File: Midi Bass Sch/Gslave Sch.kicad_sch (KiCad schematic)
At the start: 12 parts, among them J8 G SLAVE ISCP, SW6 G-slave Reset, U10 PIC16F1789

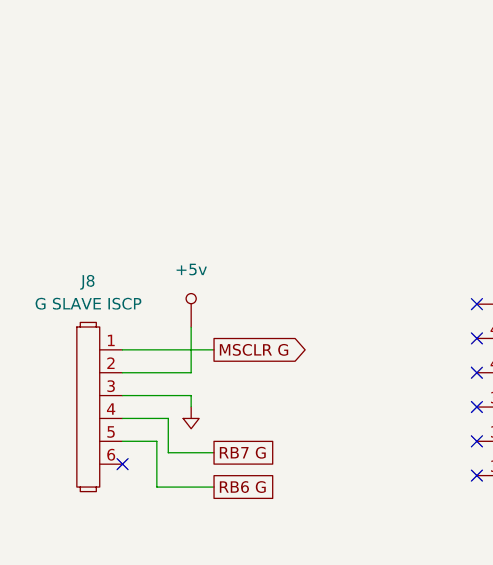
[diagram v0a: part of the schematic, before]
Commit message: working on final troubleshooting sections, modified pluck slave to header connections
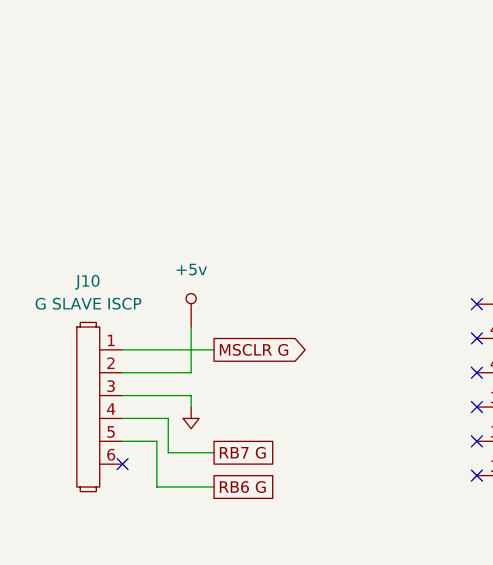
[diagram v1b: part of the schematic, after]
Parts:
- renumbered J8 to J10
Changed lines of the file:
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@@
 		(dnp no)
 		(fields_autoplaced yes)
-		(property "Reference" "J8"
+		(property "Reference" "J10"
 			(at 25.4 46.99 0)
 			(effects
@@
 			(project "Midi Bass Sch"
 				(path "/06818073-fb22-48ee-acc5-6dedd827034e/a79027be-e76c-43a0-a80a-a6c6a159c340"
-					(reference "J8")
+					(reference "J10")
 					(unit 1)
 				)
@@
 		(dnp no)
 		(fields_autoplaced yes)
-		(property "Reference" "#PWR0102"
+		(property "Reference" "#PWR0104"
 			(at 175.26 125.73 0)
 			(effects
@@
 			(project "Midi Bass Sch"
 				(path "/06818073-fb22-48ee-acc5-6dedd827034e/a79027be-e76c-43a0-a80a-a6c6a159c340"
-					(reference "#PWR0102")
+					(reference "#PWR0104")
 					(unit 1)
 				)
@@
 		(dnp no)
 		(fields_autoplaced yes)
-		(property "Reference" "#PWR099"
+		(property "Reference" "#PWR0101"
 			(at 46.99 138.43 0)
 			(effects
@@
 			(project "Midi Bass Sch"
 				(path "/06818073-fb22-48ee-acc5-6dedd827034e/a79027be-e76c-43a0-a80a-a6c6a159c340"
-					(reference "#PWR099")
+					(reference "#PWR0101")
 					(unit 1)
 				)
@@
 		(dnp no)
 		(fields_autoplaced yes)
-		(property "Reference" "#PWR0101"
+		(property "Reference" "#PWR0103"
 			(at 108.8644 20.4216 0)
 			(effects
@@
 			(project "Midi Bass Sch"
 				(path "/06818073-fb22-48ee-acc5-6dedd827034e/a79027be-e76c-43a0-a80a-a6c6a159c340"
-					(reference "#PWR0101")
+					(reference "#PWR0103")
 					(unit 1)
 				)
@@
 		(dnp no)
 		(fields_autoplaced yes)
-		(property "Reference" "#PWR098"
+		(property "Reference" "#PWR0100"
 			(at 51.7144 116.9416 0)
 			(effects
@@
 			(project "Midi Bass Sch"
 				(path "/06818073-fb22-48ee-acc5-6dedd827034e/a79027be-e76c-43a0-a80a-a6c6a159c340"
-					(reference "#PWR098")
+					(reference "#PWR0100")
 					(unit 1)
 				)
@@
 		(dnp no)
 		(fields_autoplaced yes)
-		(property "Reference" "#PWR0100"
+		(property "Reference" "#PWR0102"
 			(at 101.6 157.48 0)
 			(effects
@@
 			(project "Midi Bass Sch"
 				(path "/06818073-fb22-48ee-acc5-6dedd827034e/a79027be-e76c-43a0-a80a-a6c6a159c340"
-					(reference "#PWR0100")
+					(reference "#PWR0102")
 					(unit 1)
 				)
@@
 		(dnp no)
 		(fields_autoplaced yes)
-		(property "Reference" "#PWR096"
+		(property "Reference" "#PWR098"
 			(at 41.5544 47.0916 0)
 			(effects
@@
 			(project "Midi Bass Sch"
 				(path "/06818073-fb22-48ee-acc5-6dedd827034e/a79027be-e76c-43a0-a80a-a6c6a159c340"
-					(reference "#PWR096")
+					(reference "#PWR098")
 					(unit 1)
 				)
@@
 		(dnp no)
 		(fields_autoplaced yes)
-		(property "Reference" "#PWR095"
+		(property "Reference" "#PWR097"
 			(at 25.4 139.7 0)
 			(effects
@@
 			(project "Midi Bass Sch"
 				(path "/06818073-fb22-48ee-acc5-6dedd827034e/a79027be-e76c-43a0-a80a-a6c6a159c340"
-					(reference "#PWR095")
+					(reference "#PWR097")
 					(unit 1)
 				)
@@
 		(dnp no)
 		(fields_autoplaced yes)
-		(property "Reference" "#PWR097"
+		(property "Reference" "#PWR099"
 			(at 36.83 59.69 0)
 			(effects
@@
 			(project "Midi Bass Sch"
 				(path "/06818073-fb22-48ee-acc5-6dedd827034e/a79027be-e76c-43a0-a80a-a6c6a159c340"
-					(reference "#PWR097")
+					(reference "#PWR099")
 					(unit 1)
 				)
@@
 		(dnp no)
 		(fields_autoplaced yes)
-		(property "Reference" "#PWR0103"
+		(property "Reference" "#PWR0105"
 			(at 189.23 123.19 0)
 			(effects
@@
 			(project "Midi Bass Sch"
 				(path "/06818073-fb22-48ee-acc5-6dedd827034e/a79027be-e76c-43a0-a80a-a6c6a159c340"
-					(reference "#PWR0103")
-					(unit 1)
-				)
+					(reference "#PWR0105")
+					(unit 1)
+				)

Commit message: finished troubleshooting section
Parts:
- renumbered J10 to J12
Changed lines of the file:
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@@
 		(dnp no)
 		(fields_autoplaced yes)
-		(property "Reference" "J10"
+		(property "Reference" "J12"
 			(at 25.4 46.99 0)
 			(effects
@@
 			(project "Midi Bass Sch"
 				(path "/06818073-fb22-48ee-acc5-6dedd827034e/a79027be-e76c-43a0-a80a-a6c6a159c340"
-					(reference "J10")
+					(reference "J12")
 					(unit 1)
 				)
@@
 		(dnp no)
 		(fields_autoplaced yes)
-		(property "Reference" "#PWR0104"
+		(property "Reference" "#PWR0106"
 			(at 175.26 125.73 0)
 			(effects
@@
 			(project "Midi Bass Sch"
 				(path "/06818073-fb22-48ee-acc5-6dedd827034e/a79027be-e76c-43a0-a80a-a6c6a159c340"
-					(reference "#PWR0104")
+					(reference "#PWR0106")
 					(unit 1)
 				)
@@
 		(dnp no)
 		(fields_autoplaced yes)
-		(property "Reference" "#PWR0101"
+		(property "Reference" "#PWR0103"
 			(at 46.99 138.43 0)
 			(effects
@@
 			(project "Midi Bass Sch"
 				(path "/06818073-fb22-48ee-acc5-6dedd827034e/a79027be-e76c-43a0-a80a-a6c6a159c340"
-					(reference "#PWR0101")
+					(reference "#PWR0103")
 					(unit 1)
 				)
@@
 		(dnp no)
 		(fields_autoplaced yes)
-		(property "Reference" "#PWR0103"
+		(property "Reference" "#PWR0105"
 			(at 108.8644 20.4216 0)
 			(effects
@@
 			(project "Midi Bass Sch"
 				(path "/06818073-fb22-48ee-acc5-6dedd827034e/a79027be-e76c-43a0-a80a-a6c6a159c340"
-					(reference "#PWR0103")
+					(reference "#PWR0105")
 					(unit 1)
 				)
@@
 		(dnp no)
 		(fields_autoplaced yes)
-		(property "Reference" "#PWR0100"
+		(property "Reference" "#PWR0102"
 			(at 51.7144 116.9416 0)
 			(effects
@@
 			(project "Midi Bass Sch"
 				(path "/06818073-fb22-48ee-acc5-6dedd827034e/a79027be-e76c-43a0-a80a-a6c6a159c340"
-					(reference "#PWR0100")
+					(reference "#PWR0102")
 					(unit 1)
 				)
@@
 		(dnp no)
 		(fields_autoplaced yes)
-		(property "Reference" "#PWR0102"
+		(property "Reference" "#PWR0104"
 			(at 101.6 157.48 0)
 			(effects
@@
 			(project "Midi Bass Sch"
 				(path "/06818073-fb22-48ee-acc5-6dedd827034e/a79027be-e76c-43a0-a80a-a6c6a159c340"
-					(reference "#PWR0102")
+					(reference "#PWR0104")
 					(unit 1)
 				)
@@
 		(dnp no)
 		(fields_autoplaced yes)
-		(property "Reference" "#PWR098"
+		(property "Reference" "#PWR0100"
 			(at 41.5544 47.0916 0)
 			(effects
@@
 			(project "Midi Bass Sch"
 				(path "/06818073-fb22-48ee-acc5-6dedd827034e/a79027be-e76c-43a0-a80a-a6c6a159c340"
-					(reference "#PWR098")
+					(reference "#PWR0100")
 					(unit 1)
 				)
@@
 		(dnp no)
 		(fields_autoplaced yes)
-		(property "Reference" "#PWR097"
+		(property "Reference" "#PWR099"
 			(at 25.4 139.7 0)
 			(effects
@@
 			(project "Midi Bass Sch"
 				(path "/06818073-fb22-48ee-acc5-6dedd827034e/a79027be-e76c-43a0-a80a-a6c6a159c340"
-					(reference "#PWR097")
+					(reference "#PWR099")
 					(unit 1)
 				)
@@
 		(dnp no)
 		(fields_autoplaced yes)
-		(property "Reference" "#PWR099"
+		(property "Reference" "#PWR0101"
 			(at 36.83 59.69 0)
 			(effects
@@
 			(project "Midi Bass Sch"
 				(path "/06818073-fb22-48ee-acc5-6dedd827034e/a79027be-e76c-43a0-a80a-a6c6a159c340"
-					(reference "#PWR099")
+					(reference "#PWR0101")
 					(unit 1)
 				)
@@
 		(dnp no)
 		(fields_autoplaced yes)
-		(property "Reference" "#PWR0105"
+		(property "Reference" "#PWR0107"
 			(at 189.23 123.19 0)
 			(effects
@@
 			(project "Midi Bass Sch"
 				(path "/06818073-fb22-48ee-acc5-6dedd827034e/a79027be-e76c-43a0-a80a-a6c6a159c340"
-					(reference "#PWR0105")
-					(unit 1)
-				)
+					(reference "#PWR0107")
+					(unit 1)
+				)

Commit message: began getting images for schematic appendix
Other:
- title: (none) -> G-Slave Processor Schematic
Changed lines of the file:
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@@
 	(generator_version "8.0")
 	(paper "A")
+	(title_block
+		(title "G-Slave Processor Schematic")
+		(date "2024-12-10")
+		(rev "A")
+	)
 	(junction
 		(at 46.99 132.08)

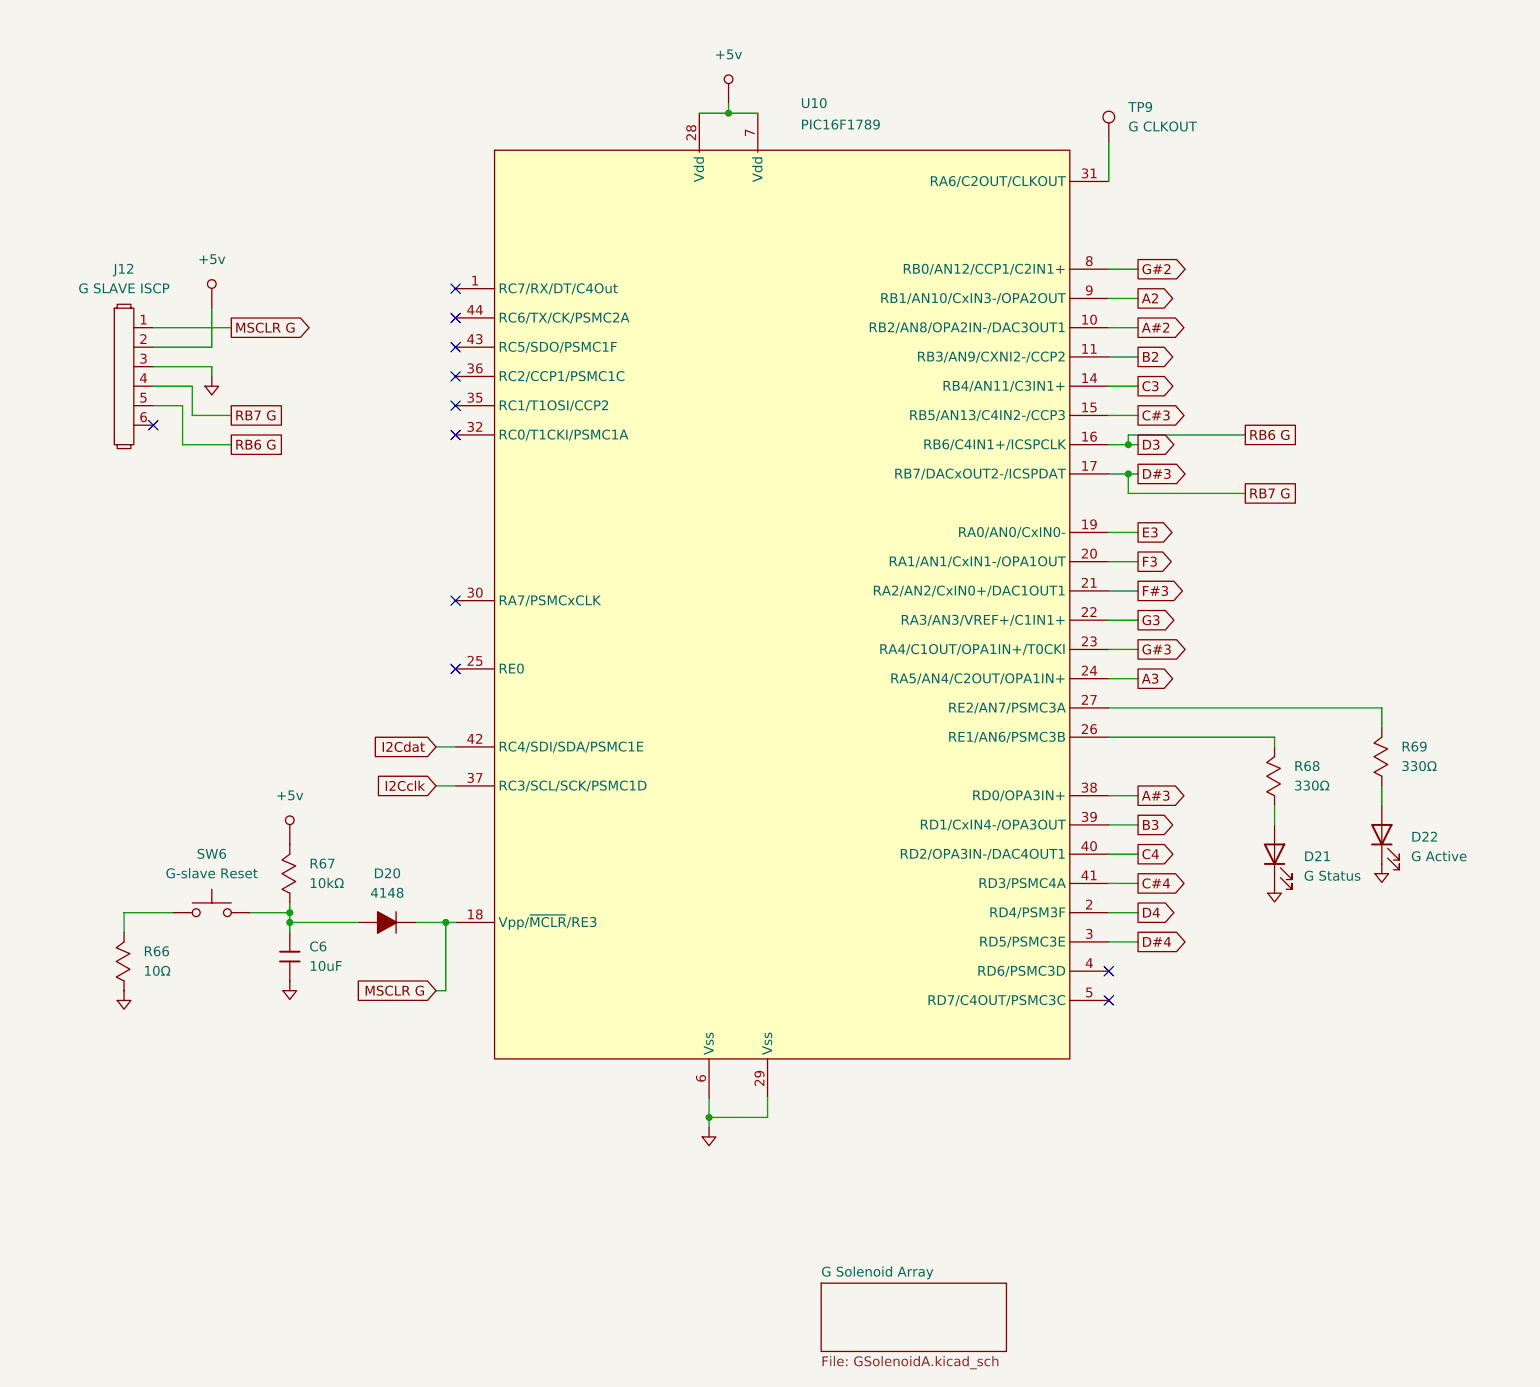
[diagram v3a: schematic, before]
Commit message: began working on pcb layout deleted extra schematics for solenoid break out board
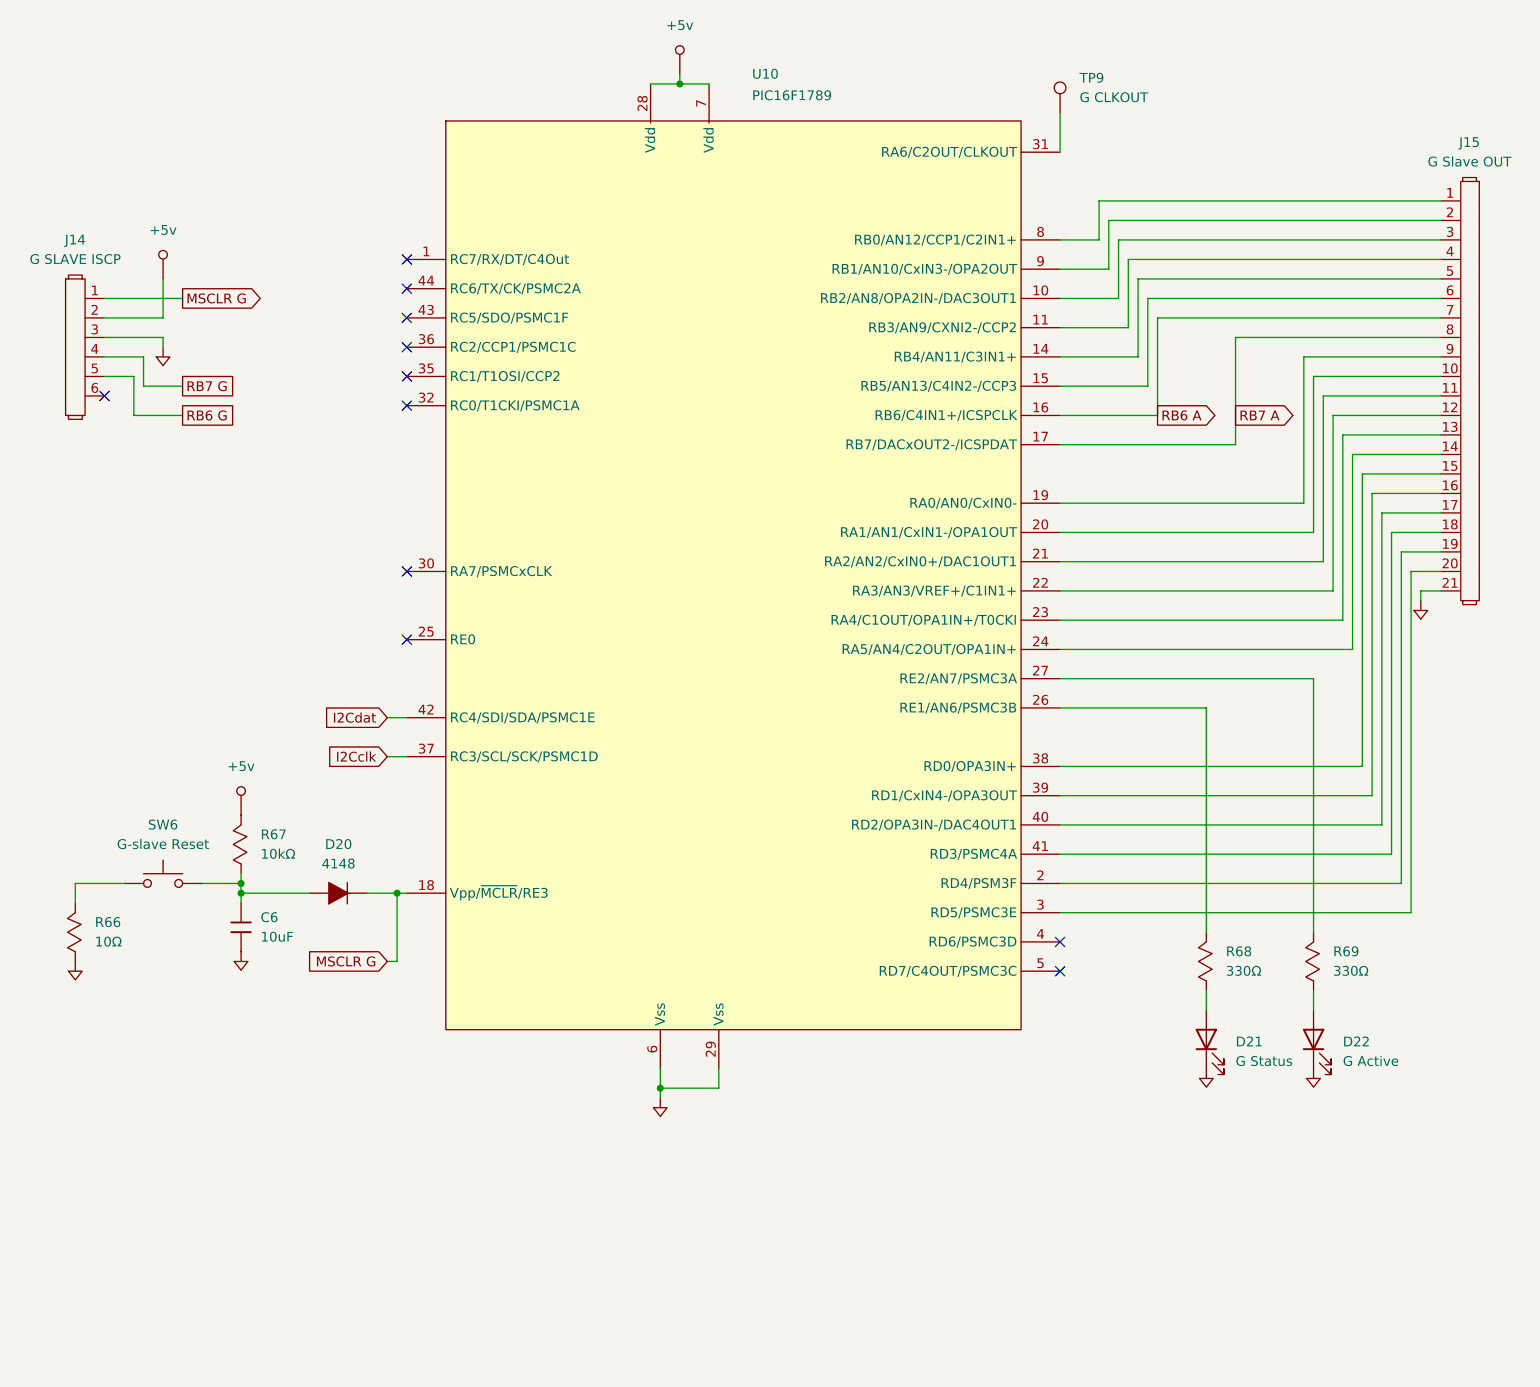
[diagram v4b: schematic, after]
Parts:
- added J15: G Slave OUT, Connector_PinHeader_2.54mm:PinHeader_1x21_P2.54mm_Vertical, symbol Owen's Symbols:Header_1x21
- SW6: footprint (none) -> Button_Switch_THT:SW_PUSH_6mm_H5mm
- TP9: footprint (none) -> Connector_PinHeader_2.54mm:PinHeader_1x01_P2.54mm_Vertical
- U10: footprint (none) -> OF footprints:TQFN-44_7x7_Pitch0.4mm
- renumbered J12 to J14
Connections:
- net GND: now also J15.21
- net A#2: no longer names the net of U10.10 (RB2/AN8/OPA2IN-/DAC3OUT1)
- net A#2: now also J15.3
- net A#3: no longer names the net of U10.38 (RD0/OPA3IN+)
- net A#3: now also J15.15
- net A2: no longer names the net of U10.9 (RB1/AN10/CxIN3-/OPA2OUT)
- net A2: now also J15.2
- net A3: no longer names the net of U10.43 (RC5/SDO/PSMC1F)
- net A3: now also J15.14
- net B2: no longer names the net of U10.11 (RB3/AN9/CXNI2-/CCP2)
- net B2: now also J15.4
- net B3: no longer names the net of U10.39 (RD1/CxIN4-/OPA3OUT)
- net B3: now also J15.16
- net C#3: no longer names the net of U10.15 (RB5/AN13/C4IN2-/CCP3)
- net C#3: now also J15.6
- net C#4: no longer names the net of U10.41 (RD3/PSMC4A)
- net C#4: now also J15.18
- net C3: no longer names the net of U10.14 (RB4/AN11/C3IN1+)
- net C3: now also J15.5
- net C4: no longer names the net of U10.40 (RD2/OPA3IN-/DAC4OUT1)
- net C4: now also J15.17
- net D#3 renamed RB7 A
- net RB7 A: now also J15.8; no longer J14.4
- net D#4: no longer names the net of U10.3 (RD5/PSMC3E)
- net D#4: now also J15.20
- net D3 renamed RB6 A
- net RB6 A: now also J15.7; no longer J14.5
- net D4: no longer names the net of U10.2 (RD4/PSM3F)
- net D4: now also J15.19
- net E3: no longer names the net of U10.32 (RC0/T1CKI/PSMC1A)
- net E3: now also J15.9
- net F#3: no longer names the net of U10.36 (RC2/CCP1/PSMC1C)
- net F#3: now also J15.11
- net F3: no longer names the net of U10.35 (RC1/T1OSI/CCP2)
- net F3: now also J15.10
- net G#2: no longer names the net of U10.8 (RB0/AN12/CCP1/C2IN1+)
- net G#2: now also J15.1
- net G#3: no longer names the net of U10.42 (RC4/SDI/SDA/PSMC1E)
- net G#3: now also J15.13
- net G3: no longer names the net of U10.37 (RC3/SCL/SCK/PSMC1D)
- net G3: now also J15.12
- new net RB6 G: J14.5
- new net RB7 G: J14.4
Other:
- removed sheet G Solenoid Array
- moved on the sheet: C6, D20, D21, D22, J14, R66, R67, R68, R69, SW6, TP9, U10

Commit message: working in finishing Rev A pcb for motherboard
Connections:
- net RB6 A is gone; now on net RB6 G: J15.7, U10.16 (RB6/C4IN1+/ICSPCLK)
- net RB7 A is gone; now on net RB7 G: J15.8, U10.17 (RB7/DACxOUT2-/ICSPDAT)
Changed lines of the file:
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@@
 		)
 	)
-	(global_label "RB7 A"
+	(global_label "RB7 G"
 		(shape output)
 		(at 170.18 66.04 0)
@@
 		)
 		(property "Intersheetrefs" "${INTERSHEET_REFS}"
-			(at 178.9709 66.04 0)
+			(at 179.1523 66.04 0)
 			(effects
 				(font
@@
 		)
 	)
-	(global_label "RB6 A"
+	(global_label "RB6 G"
 		(shape output)
 		(at 160.02 66.04 0)
@@
 		)
 		(property "Intersheetrefs" "${INTERSHEET_REFS}"
-			(at 168.8109 66.04 0)
+			(at 168.9923 66.04 0)
 			(effects
 				(font
